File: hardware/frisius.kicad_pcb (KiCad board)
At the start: 4 copper layers, 40 x 60 mm, 152 parts, among them J1 Conn_02x10_Odd_Even_Shielded, J2 Conn_02x10_Odd_Even_Shielded, J3 USB_C_Receptacle, J4 MEM2067, Q1 Q_NMOS_DGS, Q2 MBT2222ADW1T1, Q3 Q_NMOS_DGS, Q4 Q_NMOS_DGS, U1 ESP32-PICO-V3-02, U10 CP2102N-Axx-xQFN24, U11 74LVC2G126GT,115, U12 RT5789, U13 MAX8881EUT33+T, U14 PAC1934x-xJQ, U15 AP228X4BSN, U2 FXOS8700CQR1, U3 MS5637-02BA03, U4 L96-M33, U5 MAX77751, U6 LM75B, U7 MAX17048G, U8 MAX8881EUT33+T, U9 ISL54225

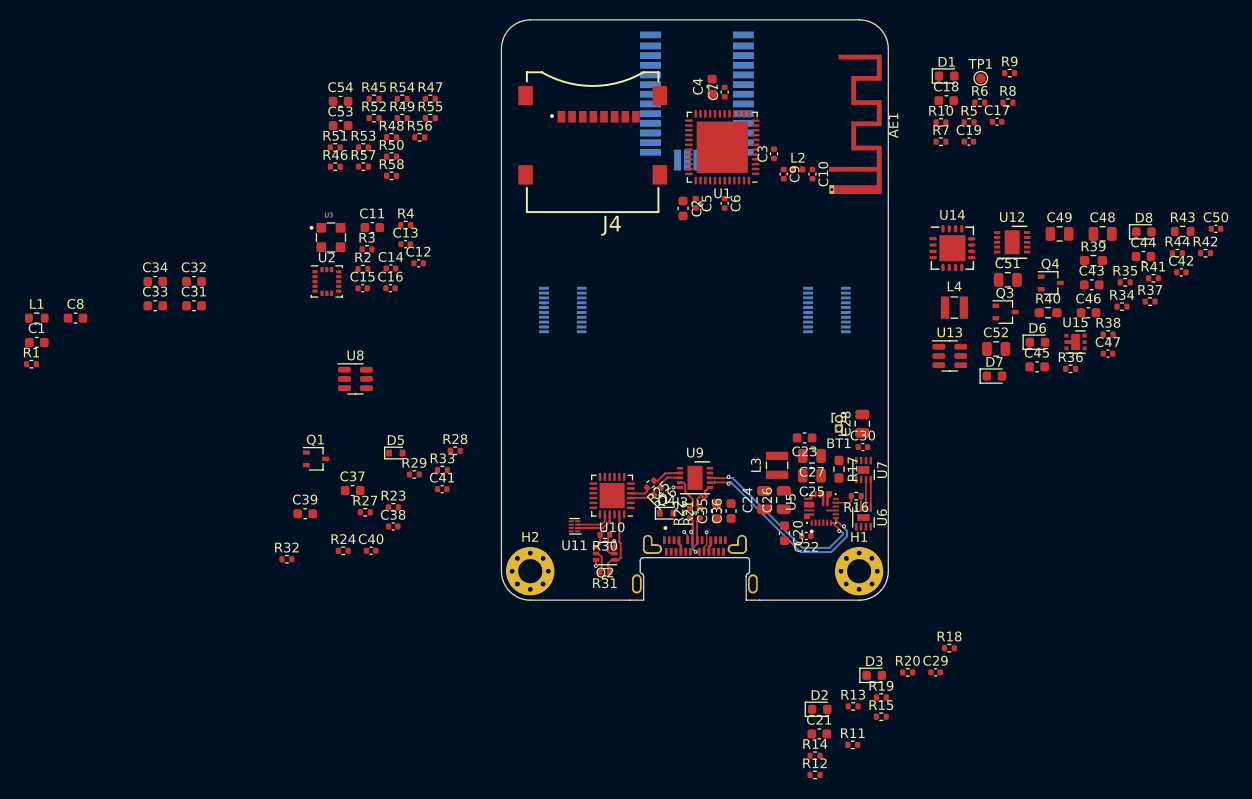
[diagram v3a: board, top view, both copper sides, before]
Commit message: initial component placement and design simplification
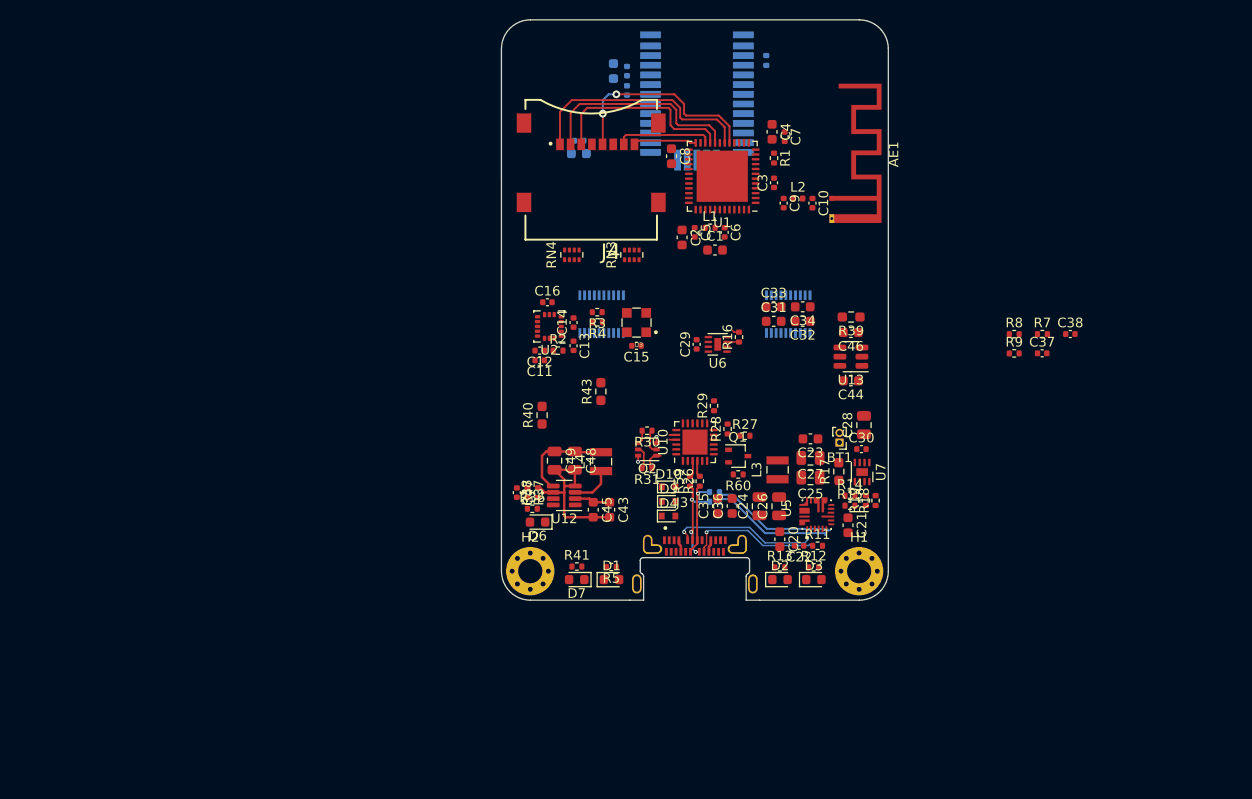
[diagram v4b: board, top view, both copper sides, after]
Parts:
- removed C39: 4.7u, Capacitor_SMD:C_0603_1608Metric
- removed C40, C41, C42, C50: 0.1u, Capacitor_SMD:C_0402_1005Metric
- removed C51, C52: 10u, Capacitor_SMD:C_0805_2012Metric
- removed D5: 3.3V, Diode_SMD:D_SOD-523
- removed D8: LED_Small_Filled, LED_SMD:LED_0603_1608Metric
- removed Q3, Q4: Q_NMOS_DGS, Package_TO_SOT_SMD:SOT-323_SC-70
- removed R10, R21, R22, R45, R46, R47, R48, R49, R50, R51: 22, Resistor_SMD:R_0402_1005Metric
- removed R20: 4.7k, Resistor_SMD:R_0402_1005Metric
- removed R23, R32, R33, R34, R35, R42: 100k, Resistor_SMD:R_0402_1005Metric
- removed R44: 1k, Resistor_SMD:R_0402_1005Metric
- removed R52, R53, R54, R55, R56, R57, R58: 10k, Resistor_SMD:R_0402_1005Metric
- removed TP1: L96_FIX, TestPoint:TestPoint_Pad_D1.0mm
- removed U11: 74LVC2G126GT,115, Package_SON:X2SON-8_1.4x1mm_P0.35mm
- removed U14: PAC1934x-xJQ, Package_DFN_QFN:UQFN-16-1EP_4x4mm_P0.65mm_EP2.7x2.7mm
- removed U15: AP228X4BSN, bt_Package_DFN:Diodes_UDFN2020-6
- removed U8: MAX8881EUT33+T, Package_TO_SOT_SMD:SOT-23-6
- removed U9: ISL54225, Package_DFN_QFN:DFN-10-1EP_3x3mm_P0.5mm_EP1.55x2.48mm
- added D10: TVS, Diode_SMD:D_SOD-523, F.Cu at (131.9, 82.2)
- added D9: TVS, Diode_SMD:D_SOD-523, F.Cu at (131.9, 83.7)
- added R59: 0, Resistor_SMD:R_0402_1005Metric, F.Cu at (134.1, 81.6)
- added R60: 100k, Resistor_SMD:R_0402_1005Metric, F.Cu at (139.1, 80.9)
- added RN3: 10k, Resistor_SMD:R_Array_Concave_4x0402, F.Cu at (128.1, 58.2)
- added RN4: 10k, Resistor_SMD:R_Array_Concave_4x0402, F.Cu at (121.9, 58.2)
- C11: footprint Capacitor_SMD:C_0603_1608Metric -> Capacitor_SMD:C_0402_1005Metric
- C17, C18, C19, C54, R6: moved to B.Cu
- C37: value 1u -> 0.1u; footprint Capacitor_SMD:C_0603_1608Metric -> Capacitor_SMD:C_0402_1005Metric
- C53: footprint Capacitor_SMD:C_0603_1608Metric -> Capacitor_SMD:C_0402_1005Metric; moved to B.Cu
- L1: footprint Resistor_SMD:R_0603_1608Metric -> Resistor_SMD:R_0402_1005Metric
- R17, R39, R40: value 10m -> 0
- R24: value 100k -> 0; moved to B.Cu
- R25: value 22 -> 0; moved to B.Cu
- R26, R7, R8, R9: value 22 -> 0
- R43: value 10m -> 0; footprint Resistor_SMD:R_0603_1608Metric -> Resistor_SMD:R_0603_1608Metric_Pad0.98x0.95mm_HandSolder
- U12: footprint Package_DFN_QFN:DFN-10-1EP_3x3mm_P0.5mm_EP1.55x2.48mm -> Package_TO_SOT_SMD:TSOT-23-8
- moved R1 79.7 mm to (142.8, 48.2), turned to -90 degrees
- moved C38 72.8 mm to (173.4, 66.4)
- moved C37 72.7 mm to (170.5, 68.4)
- moved C1 70.8 mm to (136.7, 57.7)
- moved L1 70.2 mm to (136.2, 55.4)
- moved R37 67.3 mm to (117.3, 82.8), turned to -90 degrees
- moved C34 67.0 mm to (145.8, 63.6), turned to 180 degrees
- moved R41 66.6 mm to (122.4, 90.4)
- moved C33 63.9 mm to (142.8, 63.6)
- moved C8 63.8 mm to (132.2, 48.0), turned to -90 degrees
- moved C32 63.1 mm to (145.8, 65.1), turned to 180 degrees
- moved C47 62.8 mm to (116.2, 82.8), turned to -90 degrees
- moved D1 62.5 mm to (126.0, 91.8)
- moved R43 62.4 mm to (124.9, 72.3), turned to 90 degrees
- moved R38 61.2 mm to (118.4, 82.8), turned to 90 degrees
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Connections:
- C37 pad 1: VDD_NVDC -> GND
- C37 pad 2: GND -> 3V3_CORE
- C38 pad 1: VDD_USB_3V3 -> GND
- C38 pad 2: GND -> 3V3_CORE
- J4 pad 1: Net-(J4-Pad1) -> /Processor/SDMMC.D2
- J4 pad 10: Net-(J4-Pad10) -> /Processor/SDMMC.CD
- J4 pad 2: Net-(J4-Pad2) -> /Processor/SDMMC.D3
- J4 pad 3: Net-(J4-Pad3) -> /Processor/SDMMC.CMD
- J4 pad 5: Net-(J4-Pad5) -> /Processor/SDMMC.CLK
- J4 pad 7: Net-(J4-Pad7) -> /Processor/SDMMC.D0
- J4 pad 8: Net-(J4-Pad8) -> /Processor/SDMMC.D1
- R17 pad 1: +BATT -> Net-(U5-Pad13_14)
- R17 pad 2: /BMS/I_{bat}.- -> +BATT
- R24 pad 1: Net-(Q1-Pad1) -> /USB/PORT_D-
- R24 pad 2: VDD_USB_3V3 -> /BMS/USB_CHG.D-
- R25 pad 1: /USB/CP2102N_D- -> /USB/PORT_D+
- R25 pad 2: /USB/TERM_CP2102N_D- -> /BMS/USB_CHG.D+
- R26 pad 1: /USB/CP2102N_D+ -> /USB/PORT_D-
- R26 pad 2: /USB/TERM_CP2102N_D+ -> /USB/CP2102N_D-
- R27 pad 2: VDD_USB_3V3 -> 3V3_CORE
- R28 pad 2: VDD_USB_3V3 -> 3V3_CORE
- R39 pad 1: VCC_BKUP_3V3 -> Net-(C46-Pad1)
- R39 pad 2: Net-(R39-Pad2) -> VCC_BKUP_3V3
- R40 pad 1: 3V3_CORE -> VDD_SYS_3V3
- R40 pad 2: Net-(R40-Pad2) -> 3V3_CORE
- R43 pad 1: VDD_AUX_3V3 -> VDD_SYS_3V3
- R43 pad 2: Net-(R43-Pad2) -> VDD_AUX_3V3
- R7 pad 1: /GPS/L96_SDA -> Net-(U10-Pad7)
- R7 pad 2: /BMS/SENSOR_I2C.SDA -> 3V3_CORE
- R8 pad 1: /GPS/L96_SCL -> /Processor/DEBUG_UART.RXD
- R8 pad 2: /BMS/SENSOR_I2C.SCL -> /USB/CP2102N_UART_TX
- R9 pad 1: /GPS/L96_TXD -> /Processor/DEBUG_UART.TXD
- R9 pad 2: /GPS/GPS_UART.RX -> /USB/CP2102N_UART_RX
- U1 pad 11: /Processor/GPS_UART.RX -> /GPS/GPS_UART.RX
- U1 pad 12: /Processor/GPS_UART.TX -> /GPS/GPS_UART.TX
- U1 pad 17: /Processor/SDMMC_CLK -> /Processor/SDMMC.CLK
- U1 pad 21: /Processor/SDMMC_CMD -> /Processor/SDMMC.CMD
- U1 pad 23: /Processor/SDMMC_CD -> /Processor/SDMMC.CD
- U10 pad 3: /USB/TERM_CP2102N_D+ -> /USB/CP2102N_D+
- U10 pad 4: /USB/TERM_CP2102N_D- -> /USB/CP2102N_D-
- U10 pad 5: VDD_USB_3V3 -> 3V3_CORE
- U10 pad 6: VDD_USB_3V3 -> 3V3_CORE
- U10 pad 7: VDD_USB_3V3 -> Net-(U10-Pad7)
- U12 pad 1: (no net) -> unconnected-(U12-Pad1)
- U12 pad 2: GND -> VDD_NVDC
- U12 pad 4: unconnected-(U12-Pad4) -> GND
- U3 pad 1: (no net) -> VDD_AUX_3V3
- U3 pad 2: (no net) -> /BMS/SENSOR_I2C.SDA
- U3 pad 3: (no net) -> /BMS/SENSOR_I2C.SCL
- U3 pad 4: (no net) -> Net-(C15-Pad2)
- U4 pad 2: Net-(TP1-Pad1) -> unconnected-(U4-Pad2)
- U4 pad 25: /GPS/L96_TXD -> /GPS/GPS_UART.RX
- U4 pad 26: /GPS/L96_RXD -> /GPS/GPS_UART.TX
- U4 pad 3: /GPS/L96_SDA -> unconnected-(U4-Pad3)
- U4 pad 6: /GPS/L96_SCL -> unconnected-(U4-Pad6)
- U5 pad 13_14: Net-(R17-Pad4) -> Net-(U5-Pad13_14)
- U7 pad 5: Net-(R20-Pad2) -> unconnected-(U7-Pad5)
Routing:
- net /Processor/SDMMC.D2: track 0.00 -> 24.2 mm
- net /Processor/SDMMC.D3: track 0.00 -> 21.8 mm
- net /Processor/SDMMC.CLK: track 0.00 -> 21.6 mm, vias 0 -> 2
- net /Processor/SDMMC.CMD: track 0.00 -> 19.7 mm
- net GND: track 0.67 -> 17.7 mm, vias 1 -> 0
- net /BMS/USB_CC.1: track 0.99 -> 15.0 mm
- net /BMS/USB_CC.2: track 2.13 -> 13.6 mm
- net VDD_SYS_3V3: track 0.00 -> 10.1 mm
- net /Processor/SDMMC.D0: track 0.00 -> 9.97 mm
- net /BMS/USB_CHG.D-: track 20.4 -> 13.1 mm, vias 2 -> 0
- net /BMS/USB_CHG.D+: track 19.3 -> 12.7 mm, vias 2 -> 0
- net /Processor/SDMMC.D1: track 0.00 -> 6.57 mm
- net /USB/PORT_D+: track 5.27 -> 11.2 mm, vias 2 -> 3
- net Net-(Q2-Pad1): track 7.09 -> 2.25 mm
- net /USB/PORT_D-: track 3.77 -> 8.59 mm, vias 0 -> 1
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
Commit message: fixing submodule
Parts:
- removed AE1: 2.4G, RF_Antenna:Texas_SWRA117D_2.4GHz_Left
- removed J2: Conn_02x10_Odd_Even_Shielded, Connector_Molex:Molex_SlimStack_55560-0201_2x10_P0.50mm_Vertical
- removed R60: 100k, Resistor_SMD:R_0402_1005Metric
- removed RN3, RN4: 10k, Resistor_SMD:R_Array_Concave_4x0402
- added C39: 0.1u, Capacitor_SMD:C_0402_1005Metric, F.Cu at (183.4, 77.0)
- added C40: 1u, Capacitor_SMD:C_0603_1608Metric, F.Cu at (183.9, 74.8)
- added D5: MBR0540, LED_SMD:LED_0603_1608Metric, F.Cu at (164.8, 76.0)
- added R10: 1k, Resistor_SMD:R_0402_1005Metric, F.Cu at (168.3, 75.7)
- added R20: 0, Resistor_SMD:R_0805_2012Metric, F.Cu at (191.7, 82.2)
- added R21: 1k, Resistor_SMD:R_0402_1005Metric, F.Cu at (167.1, 85.7)
- added R23: 0, Resistor_SMD:R_0402_1005Metric, F.Cu at (191.0, 74.5)
- added R32: 22, Resistor_SMD:R_0402_1005Metric, F.Cu at (135.6, 59.7)
- added R33: 22, Resistor_SMD:R_0402_1005Metric, F.Cu at (133.2, 54.3)
- added R34: 22, Resistor_SMD:R_0402_1005Metric, F.Cu at (133.2, 53.3)
- added R35: 22, Resistor_SMD:R_0402_1005Metric, F.Cu at (135.6, 57.7)
- added R42: 22, Resistor_SMD:R_0402_1005Metric, F.Cu at (133.2, 56.3)
- added R44: 10k, Resistor_SMD:R_0402_1005Metric, F.Cu at (162.8, 45.7)
- added R45: 10k, Resistor_SMD:R_0402_1005Metric, F.Cu at (164.0, 54.7)
- added R46: 10k, Resistor_SMD:R_0402_1005Metric, F.Cu at (166.9, 50.8)
- added R47: 10k, Resistor_SMD:R_0402_1005Metric, F.Cu at (172.7, 50.8)
- added R48: 10k, Resistor_SMD:R_0402_1005Metric, F.Cu at (169.8, 50.8)
- added R49: 10k, Resistor_SMD:R_0402_1005Metric, F.Cu at (161.1, 54.7)
- added SW1: OVERRIDE, Button_Switch_SMD:SW_DIP_SPSTx04_Slide_Copal_CHS-04A_W5.08mm_P1.27mm_JPin, F.Cu at (124.2, 89.9)
- added SW2: SW_Push, Button_Switch_SMD:SW_SPST_B3U-1000P, F.Cu at (177.3, 94.5)
- added SW3: SW_Push, Button_Switch_SMD:SW_SPST_B3U-1000P, F.Cu at (185.5, 86.5)
- added SW4: SW_Push, Button_Switch_SMD:SW_SPST_B3U-1000P, F.Cu at (183.1, 94.5)
- C31, C32, C33, C34: value 4.7u -> 1u
- D6: value MBR0540 -> LED_Small_Filled
- D7: value LED_Small_Filled -> SK6805; footprint LED_SMD:LED_0603_1608Metric -> LED_SMD:LED_SK6805_PLCC4_2.4x2.7mm_P1.3mm
- J1: value Conn_02x10_Odd_Even_Shielded -> Conn_02x20_Odd_Even_Shielded; footprint Connector_Molex:Molex_SlimStack_55560-0201_2x10_P0.50mm_Vertical -> Connector_Molex:Molex_SlimStack_502426-4010_2x20_P0.40mm_Vertical; moved to F.Cu
- J4: moved to B.Cu
- R12: value 1k -> 100k
- R17, R40, R43: footprint Resistor_SMD:R_0603_1608Metric_Pad0.98x0.95mm_HandSolder -> Resistor_SMD:R_0805_2012Metric
- R27: value 100k -> 0
- R41: value 1k -> 22
- moved D7 59.4 mm to (179.5, 75.5), turned to 0 degrees
- moved D6 53.7 mm to (170.5, 72.7), turned to 0 degrees
- moved R27 51.2 mm to (191.0, 76.5)
- moved J1 46.1 mm to (171.0, 62.0)
- moved C31 41.3 mm to (183.7, 71.0)
- moved C33 41.2 mm to (183.7, 68.5)
- moved R41 36.7 mm to (133.2, 55.3), turned to 180 degrees
- moved D1 36.0 mm to (162.0, 93.5)
- moved R5 36.0 mm to (161.9, 92.2)
- moved C34 34.7 mm to (179.6, 71.0), turned to 0 degrees
- moved C32 34.0 mm to (179.6, 68.5), turned to 0 degrees
- moved R13 27.3 mm to (170.0, 84.6)
- moved R12 26.1 mm to (171.6, 82.0)
- moved Q1 25.0 mm to (163.8, 82.9)
- moved D3 23.2 mm to (168.1, 82.3)
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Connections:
- net /Processor/3V3_CORE_EN renamed /Processor/POWER_EN
- net /Processor/VDD_AUX_EN renamed /Processor/SPARE1
- net Net-(Q2-Pad1) renamed /USB/CP2102N_DTR
- net Net-(Q2-Pad2) renamed /USB/~{RTS}_BASE
- net Net-(Q2-Pad4) renamed /USB/CP2102N_RTS
- net Net-(Q2-Pad5) renamed /USB/DTR_BASE
- net Net-(R29-Pad1) renamed /USB/CP2102N_~{SUS}
- C31 pad 1: VCC_BKUP_3V3 -> VDD_DISP_3V3
- C31 pad 2: GND -> Net-(J1-Pad1)
- C32 pad 1: VDD_AUX_3V3 -> VCC_BKUP_3V3
- C32 pad 2: GND -> Net-(J1-Pad1)
- C33 pad 1: VDD_NVDC -> VDD_DISP_3V3
- C33 pad 2: GND -> Net-(J1-Pad1)
- C34 pad 1: VDD_NVDC -> VCC_BKUP_3V3
- C34 pad 2: GND -> Net-(J1-Pad1)
- C37 pad 2: 3V3_CORE -> VDD_USB_3V3
- C38 pad 2: 3V3_CORE -> VDD_USB_3V3
- C47 pad 1: VDD_SYS_3V3 -> Net-(C47-Pad1)
- C48 pad 1: VDD_SYS_3V3 -> Net-(C47-Pad1)
- C49 pad 1: VDD_SYS_3V3 -> Net-(C47-Pad1)
- D2 pad 2: 3V3_CORE -> VDD_USB_3V3
- D3 pad 2: 3V3_CORE -> VDD_USB_3V3
- D6 pad 1: /Power/PWR_CTRL.CORE_EN -> Net-(D6-Pad1)
- D6 pad 2: /Display B2B/USR_BTN.PWR -> Net-(C47-Pad1)
- D7 pad 1: Net-(D7-Pad1) -> /User Interface/STATUS_LED_EXT
- D7 pad 2: 3V3_CORE -> GND
- J1 pad 1: GND -> Net-(J1-Pad1)
- J1 pad 10: /Display B2B/USR_BTN.PWR -> VDD_DISP_3V3
- J1 pad 11: /Display B2B/DISPLAY.SCLK -> Net-(J1-Pad1)
- J1 pad 12: GND -> Net-(J1-Pad1)
- J1 pad 13: /Display B2B/DISPLAY.CS -> Net-(J1-Pad1)
- J1 pad 14: GND -> Net-(J1-Pad1)
- J1 pad 15: /Display B2B/DISPLAY.DC -> /Display B2B/STATUS_LED_EXT
- J1 pad 16: /BMS/SENSOR_I2C.SDA -> /Display B2B/SPARE_0
- J1 pad 17: /Display B2B/DISPLAY.BL -> Net-(J1-Pad1)
- J1 pad 18: /BMS/SENSOR_I2C.SCL -> /Display B2B/SPARE_1
- J1 pad 19: GND -> /Display B2B/DISPLAY.MOSI
- J1 pad 2: GND -> Net-(J1-Pad1)
- J1 pad 20: GND -> /Display B2B/SPARE_2
- J1 pad 3: /Processor/STATUS_LED -> Net-(J1-Pad1)
- J1 pad 4: /Display B2B/VDD_CORE_EN -> Net-(J1-Pad1)
- J1 pad 5: GND -> VDD_DISP_3V3
- J1 pad 6: GND -> VDD_DISP_3V3
- J1 pad 7: /Display B2B/DISPLAY.MOSI -> VDD_DISP_3V3
- J1 pad 8: /Display B2B/USR_BTN.NAV_A -> VDD_DISP_3V3
- J1 pad 9: /Display B2B/DISPLAY.MISO -> VDD_DISP_3V3
- J4 pad 1: /Processor/SDMMC.D2 -> Net-(J4-Pad1)
- J4 pad 10: /Processor/SDMMC.CD -> GND
- J4 pad 2: /Processor/SDMMC.D3 -> Net-(J4-Pad2)
- J4 pad 3: /Processor/SDMMC.CMD -> Net-(J4-Pad3)
- J4 pad 5: /Processor/SDMMC.CLK -> Net-(J4-Pad5)
- J4 pad 7: /Processor/SDMMC.D0 -> Net-(J4-Pad7)
- J4 pad 8: /Processor/SDMMC.D1 -> Net-(J4-Pad8)
- L4 pad 2: VDD_SYS_3V3 -> Net-(C47-Pad1)
- Q1 pad 1: Net-(Q1-Pad1) -> /Processor/USB_PRESENT
- Q1 pad 2: /Processor/USB_PRESENT -> Net-(R11-Pad1)
- R11 pad 1: /Processor/USB_PRESENT -> Net-(R11-Pad1)
- R11 pad 2: 3V3_CORE -> VDD_USB_3V3
- R12 pad 1: Net-(D3-Pad1) -> /Processor/USB_PRESENT
- R12 pad 2: /Processor/USB_PRESENT -> VDD_USB_3V3
- R13 pad 1: Net-(D2-Pad1) -> Net-(R11-Pad1)
- R13 pad 2: Net-(R13-Pad2) -> Net-(D2-Pad1)
- R27 pad 1: Net-(Q1-Pad1) -> Net-(U4-Pad6)
- R27 pad 2: 3V3_CORE -> /BMS/SENSOR_I2C.SCL
- R28 pad 2: 3V3_CORE -> VDD_USB_3V3
- R36 pad 1: VDD_SYS_3V3 -> /Power/POWER_EN
- R36 pad 2: /Power/PWR_CTRL.CORE_EN -> Net-(C47-Pad1)
- R37 pad 1: VDD_SYS_3V3 -> Net-(C47-Pad1)
- R40 pad 1: VDD_SYS_3V3 -> Net-(C47-Pad1)
- R41 pad 1: GND -> /Processor/SDMMC.D0
- R41 pad 2: Net-(D7-Pad1) -> Net-(J4-Pad7)
- R7 pad 2: 3V3_CORE -> VDD_USB_3V3
- U1 pad 23: /Processor/SDMMC.CD -> /Processor/SPARE2
- U1 pad 7: unconnected-(U1-Pad7) -> /Processor/SPARE0
- U10 pad 5: 3V3_CORE -> VDD_USB_3V3
- U10 pad 6: 3V3_CORE -> VDD_USB_3V3
- U10 pad 8: Net-(Q1-Pad1) -> /Processor/USB_PRESENT
- U12 pad 5: VDD_SYS_3V3 -> Net-(C47-Pad1)
- U12 pad 8: /Power/PWR_CTRL.CORE_EN -> /Power/POWER_EN
- U4 pad 2: unconnected-(U4-Pad2) -> Net-(U4-Pad2)
- U4 pad 23: unconnected-(U4-Pad23) -> Net-(U4-Pad23)
- U4 pad 28: unconnected-(U4-Pad28) -> Net-(U4-Pad28)
- U4 pad 3: unconnected-(U4-Pad3) -> Net-(U4-Pad3)
- U4 pad 6: unconnected-(U4-Pad6) -> Net-(U4-Pad6)
- U4 pad 7: unconnected-(U4-Pad7) -> Net-(U4-Pad7)
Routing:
- net /Processor/SDMMC.D2: track 24.2 -> 0.00 mm
- net /Processor/SDMMC.D3: track 21.8 -> 0.00 mm
- net /Processor/SDMMC.CLK: track 21.6 -> 0.00 mm, vias 2 -> 0
- net /Processor/SDMMC.CMD: track 19.7 -> 0.00 mm
- net Net-(C47-Pad1): track 0.00 -> 10.1 mm
- net VDD_SYS_3V3: track 10.1 -> 0.00 mm
- net /Processor/SDMMC.D0: track 9.97 -> 0.00 mm
- net /Processor/SDMMC.D1: track 6.57 -> 0.00 mm
